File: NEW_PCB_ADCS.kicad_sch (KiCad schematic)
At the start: 9 parts, among them J4 SWD

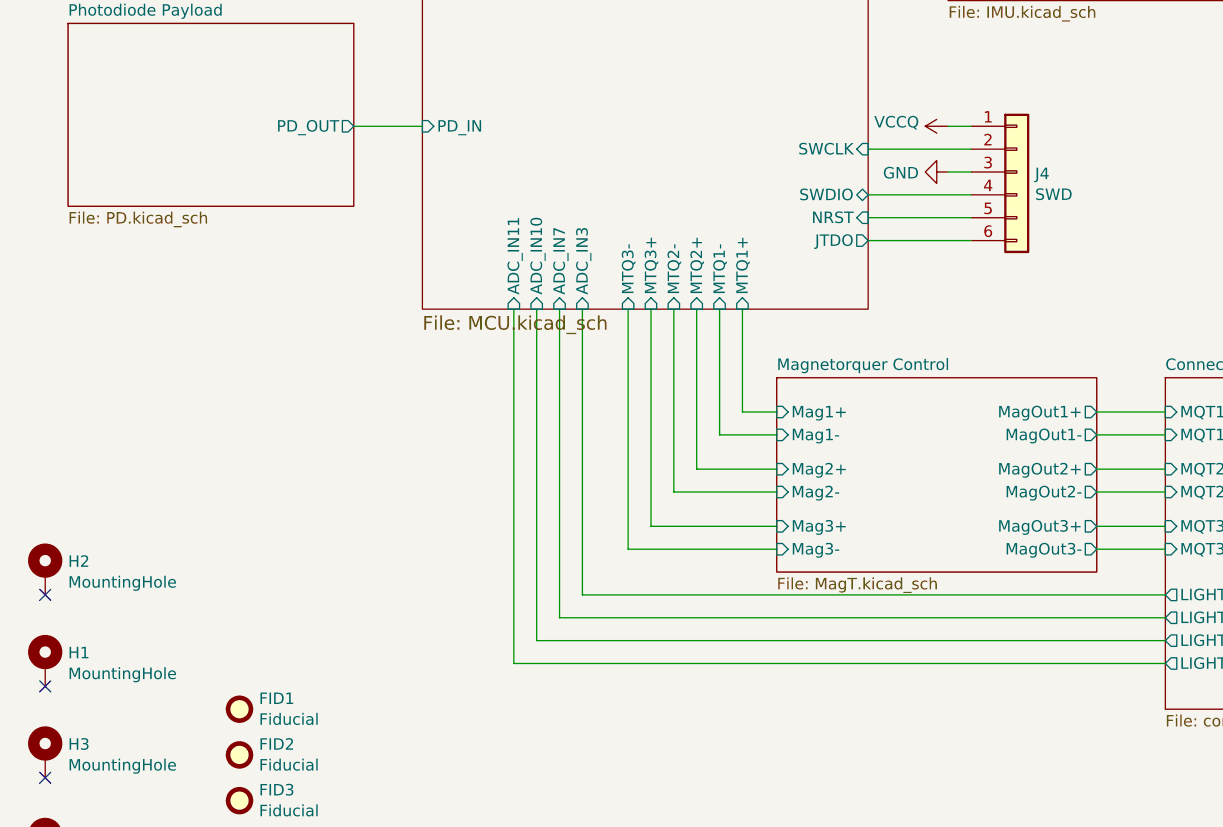
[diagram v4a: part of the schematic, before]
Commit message: Reannotate schematic
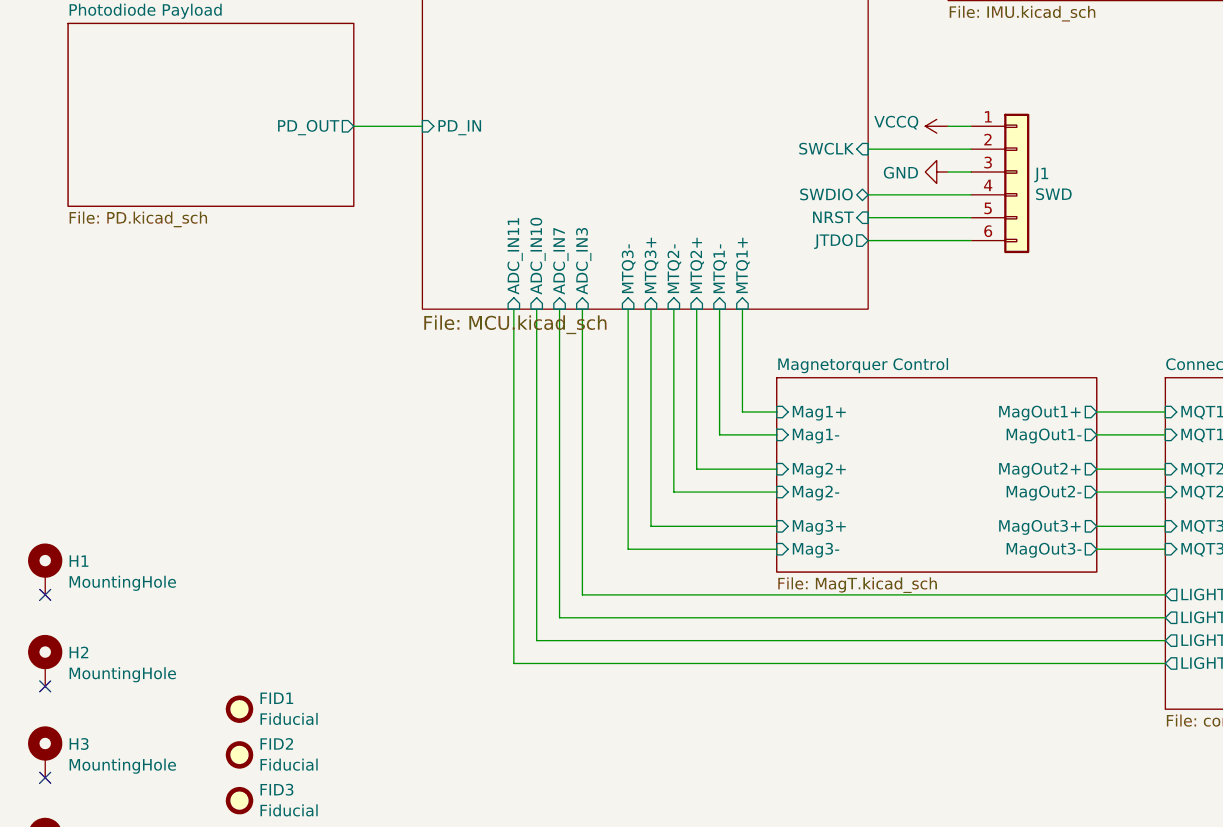
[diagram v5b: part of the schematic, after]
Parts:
- renumbered H2 to H1, H1 to H2, J4 to J1
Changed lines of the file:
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@@
   (symbol (lib_id "Connector_Generic:Conn_01x06") (at 129.54 109.22 0) (unit 1)
     (in_bom yes) (on_board yes) (dnp no)
-    (property "Reference" "J4" (at 131.572 109.4232 0)
+    (property "Reference" "J1" (at 131.572 109.4232 0)
       (effects (font (size 1.27 1.27)) (justify left))
     )
@@
       (project "NEW_PCB_ADCS"
         (path "/42c40d7d-71af-4ce9-bac9-d638f259c957"
-          (reference "J4") (unit 1)
+          (reference "J1") (unit 1)
         )
       )
@@
   (symbol (lib_id "power:GND") (at 121.92 109.22 270) (unit 1)
     (in_bom yes) (on_board yes) (dnp no)
-    (property "Reference" "#PWR059" (at 115.57 109.22 0)
+    (property "Reference" "#PWR02" (at 115.57 109.22 0)
       (effects (font (size 1.27 1.27)) hide)
     )
@@
       (project "NEW_PCB_ADCS"
         (path "/42c40d7d-71af-4ce9-bac9-d638f259c957"
-          (reference "#PWR059") (unit 1)
+          (reference "#PWR02") (unit 1)
         )
       )
@@
   (symbol (lib_id "power:VCCQ") (at 121.92 104.14 90) (unit 1)
     (in_bom yes) (on_board yes) (dnp no)
-    (property "Reference" "#PWR0105" (at 125.73 104.14 0)
+    (property "Reference" "#PWR01" (at 125.73 104.14 0)
       (effects (font (size 1.27 1.27)) hide)
     )
@@
       (project "NEW_PCB_ADCS"
         (path "/42c40d7d-71af-4ce9-bac9-d638f259c957"
-          (reference "#PWR0105") (unit 1)
+          (reference "#PWR01") (unit 1)
         )
       )
@@
   (symbol (lib_id "Mechanical:MountingHole_Pad") (at 21.59 163.83 0) (unit 1)
     (in_bom yes) (on_board yes) (dnp no)
-    (property "Reference" "H1" (at 24.13 162.6616 0)
+    (property "Reference" "H2" (at 24.13 162.6616 0)
       (effects (font (size 1.27 1.27)) (justify left))
     )
@@
       (project "NEW_PCB_ADCS"
         (path "/42c40d7d-71af-4ce9-bac9-d638f259c957"
-          (reference "H1") (unit 1)
+          (reference "H2") (unit 1)
         )
       )
@@
   (symbol (lib_id "Mechanical:MountingHole_Pad") (at 21.59 153.67 0) (unit 1)
     (in_bom yes) (on_board yes) (dnp no)
-    (property "Reference" "H2" (at 24.13 152.5016 0)
+    (property "Reference" "H1" (at 24.13 152.5016 0)
       (effects (font (size 1.27 1.27)) (justify left))
     )
@@
       (project "NEW_PCB_ADCS"
         (path "/42c40d7d-71af-4ce9-bac9-d638f259c957"
-          (reference "H2") (unit 1)
+          (reference "H1") (unit 1)
         )
       )

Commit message: Update wrong MPNs
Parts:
- J1: Part Number SM06B-SRSS-TB -> 53261-0671
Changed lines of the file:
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@@
       (effects (font (size 1.27 1.27)) hide)
     )
-    (property "Part Number" "SM06B-SRSS-TB" (at -72.39 215.9 0)
+    (property "Part Number" "53261-0671" (at -72.39 215.9 0)
       (effects (font (size 1.27 1.27)) hide)
     )

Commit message: Add ChipSat inhibit
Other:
- sheet Connectors ports: added INHIBIT; removed none
- sheet MCU ports: added INHIBIT; removed none
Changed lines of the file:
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@@
+    (stroke (width 0) (type default))
+  )
+  (wire (pts (xy 69.85 167.64) (xy 146.05 167.64))
     (stroke (width 0) (type default))
   )
@@
   )
   (wire (pts (xy 55.88 50.8) (xy 63.5 50.8))
+    (stroke (width 0) (type default))
+  )
+  (wire (pts (xy 69.85 124.46) (xy 69.85 167.64))
     (stroke (width 0) (type default))
   )
@@
       (effects (font (size 1.27 1.27)) (justify left))
     )
+    (pin "INHIBIT" input (at 69.85 124.46 270)
+      (effects (font (size 1.27 1.27)) (justify left))
+    )
     (instances
       (project "pq9ish-main-hw"
@@
     )
   )
-  (sheet (at 146.05 132.08) (size 19.05 36.83) (fields_autoplaced)
+  (sheet (at 146.05 132.08) (size 19.05 38.1) (fields_autoplaced)
     (stroke (width 0.1524) (type solid))
     (fill (color 0 0 0 0.0000))
@@
       (effects (font (size 1.27 1.27)) (justify left bottom))
     )
-    (property "Sheetfile" "connectors.kicad_sch" (at 146.05 169.4946 0)
+    (property "Sheetfile" "connectors.kicad_sch" (at 146.05 170.7646 0)
       (effects (font (size 1.27 1.27)) (justify left top))
     )
@@
       (effects (font (size 1.27 1.27)) (justify left))
     )
+    (pin "INHIBIT" input (at 146.05 167.64 180)
+      (effects (font (size 1.27 1.27)) (justify left))
+    )
